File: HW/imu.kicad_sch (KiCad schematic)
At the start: 0 parts

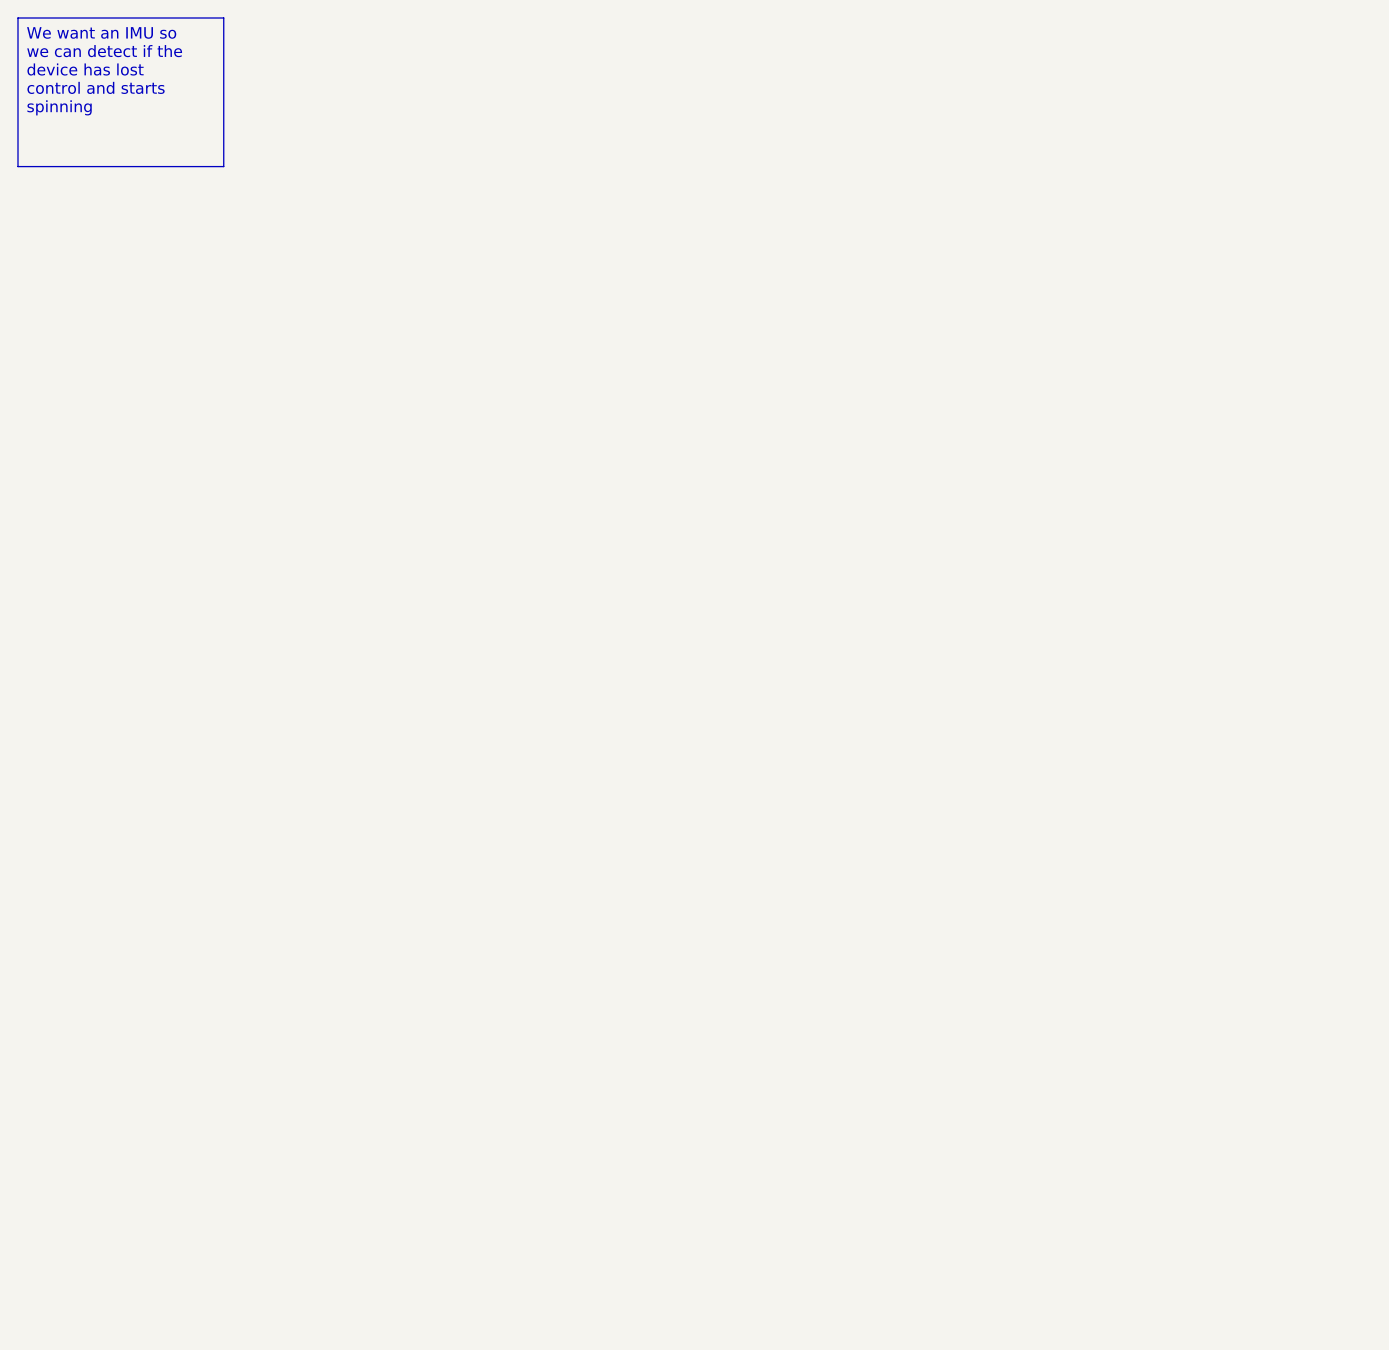
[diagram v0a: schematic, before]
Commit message: Almost first schematic draft (missing resistor values for STDRIVE current sensing and leds)
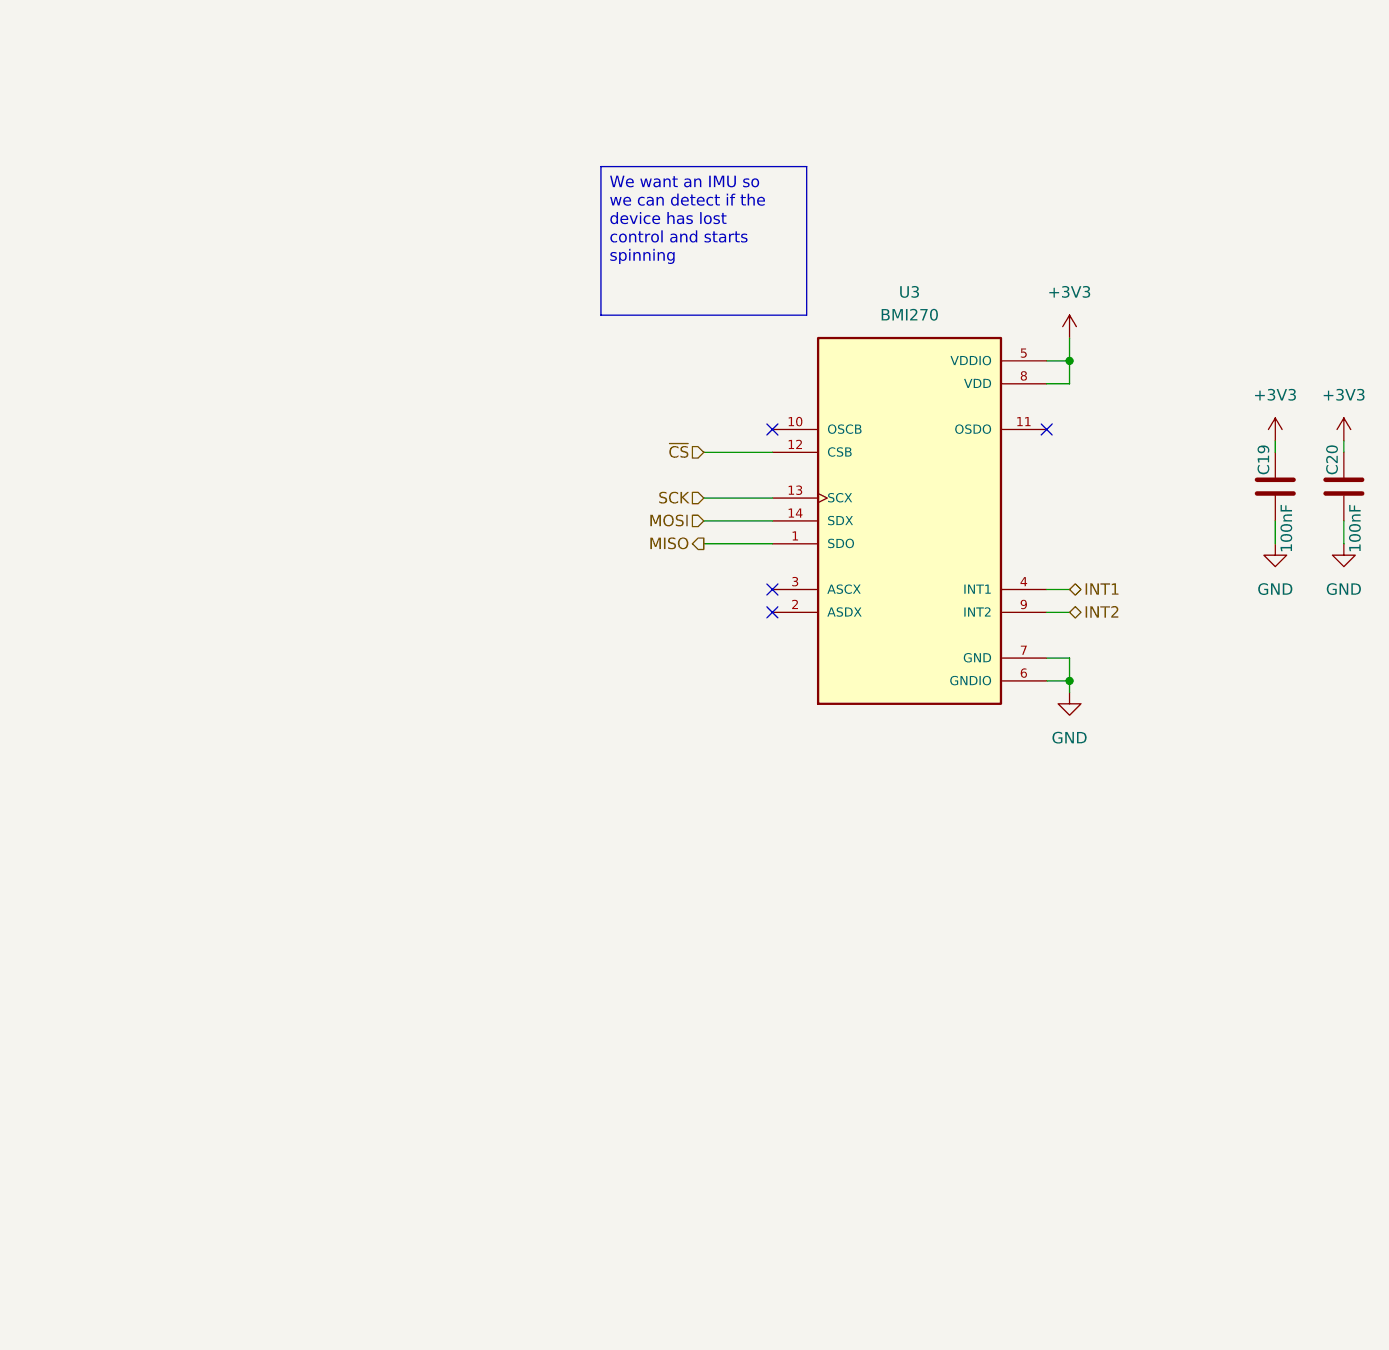
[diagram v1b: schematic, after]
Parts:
- added C19, C20: 100nF, Capacitor_SMD:C_0402_1005Metric, symbol Device:C
- added U3: BMI270, lib:XDCR_BMI270, symbol BMI270:BMI270
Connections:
- new net +3V3: C19.1, C20.1, U3.5 (VDDIO), U3.8 (VDD)
- new net GND: C19.2, C20.2, U3.6 (GNDIO), U3.7 (GND)
- new net INT1: U3.4 (INT1)
- new net INT2: U3.9 (INT2)
- new net MISO: U3.1 (SDO)
- new net MOSI: U3.14 (SDX)
- new net SCK: U3.13 (SCX)
- new net ~{CS}: U3.12 (CSB)
- no-connect marks 0 -> 4

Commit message: Cleaned up and implemented some of Laimonas' feedback
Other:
- company: (none) -> Roberto Holmes
- title: (none) -> Capstan
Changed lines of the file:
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@@
 	(generator_version "9.0")
 	(paper "A4")
+	(title_block
+		(title "Capstan")
+		(date "2025-09-26")
+		(company "Roberto Holmes")
+	)
 	(text_box "We want an IMU so we can detect if the device has lost control and starts spinning"
 		(exclude_from_sim no)
-		(at 105.41 52.07 0)
-		(size 22.86 16.51)
+		(at 153.67 166.37 0)
+		(size 22.86 15.24)
 		(margins 0.9525 0.9525 0.9525 0.9525)
 		(stroke
